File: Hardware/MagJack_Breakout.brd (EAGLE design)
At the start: 160 x 100 mm, 3 parts, among them J1 MAGJACK-NOLABELS

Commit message: Completed revised layout for prototypes
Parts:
- added FID1, FID2: FIDUCIAL1X2, SparkFun-Aesthetics:FIDUCIAL-1X2
- added LOGO1: OSHW-LOGOS, SparkFun-Aesthetics:OSHW-LOGO-S
- added LOGO2: SFE_LOGO_FLAME.1_INCH, SparkFun-Aesthetics:SFE_LOGO_FLAME_.1
- added LOGO3: SFE_LOGO_NAME_FLAME.1_INCH, SparkFun-Aesthetics:SFE_LOGO_NAME_FLAME_.1
- added STANDOFF3, STANDOFF5: STAND-OFF, SparkFun-Electromechanical:STAND-OFF
- moved J1 143.3 mm to (24.1, 25.4), turned to 180 degrees
- moved JP1 97.9 mm to (1.27, 1.27)
- moved FRAME1 80.1 mm to (-17.8, -10.2)
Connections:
- new net G+: J1.11, JP1.3
- new net G-: J1.12, JP1.2
- new net P1: J1.1, JP1.13
- new net P2: J1.2, JP1.12
- new net P3: J1.3, JP1.11
- new net P4: J1.4, JP1.10
- new net P5: J1.5, JP1.9
- new net P6: J1.6, JP1.8
- new net P7: J1.7, JP1.7
- new net P8: J1.8, JP1.6
- new net SH: J1.M1, J1.M2, JP1.1
- new net Y+: J1.9, JP1.5
- new net Y-: J1.10, JP1.4
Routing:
- net SH: track 0.00 -> 31.5 mm
- net Y+: track 0.00 -> 25.0 mm
- net Y-: track 0.00 -> 22.7 mm
- net G+: track 0.00 -> 20.4 mm
- net G-: track 0.00 -> 19.6 mm
- net P1: track 0.00 -> 13.6 mm
- net P3: track 0.00 -> 13.1 mm
- net P2: track 0.00 -> 11.2 mm
- net P5: track 0.00 -> 10.4 mm
- net P4: track 0.00 -> 9.42 mm
- net P7: track 0.00 -> 8.00 mm
- net P6: track 0.00 -> 6.28 mm
- net P8: track 0.00 -> 4.93 mm
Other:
- board size 160 x 100 mm -> 33 x 20.3 mm
- board text added: "G+"
- board text added: "G-"
- board text added: "P1"
- board text added: "P2\"
- board text added: "P3"
- board text added: "P4"
- board text added: "P5"
- board text added: "P6"
- board text added: "P7"
- board text added: "P8"
- board text added: "RJ45 MagJack Breakout"
- board text added: "Revised by Shawn Hymel"
- board text added: "SH"
- board text added: "Y+"
- board text added: "Y-"
- board text added: "v11"

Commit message: Added Nate as original designer
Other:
- board text added: "N. Seidle Revised by Shawn Hymel"
- board text removed: "Revised by Shawn Hymel"
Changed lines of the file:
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@@
 <text x="3.81" y="2.794" size="1.016" layer="21" font="vector" ratio="15" align="bottom-center">G-</text>
 <text x="1.27" y="2.794" size="1.016" layer="21" font="vector" ratio="15" align="bottom-center">SH</text>
-<text x="12.7" y="-10.3378" size="1.778" layer="51" font="vector">Revised by Shawn Hymel</text>
+<text x="12.7" y="-12.8778" size="1.778" layer="51" font="vector">N. Seidle
+Revised by Shawn Hymel</text>
 <text x="31.75" y="2.794" size="1.016" layer="22" font="vector" ratio="15" rot="MR0" align="bottom-center">P1</text>
 <text x="29.21" y="2.794" size="1.016" layer="22" font="vector" ratio="15" rot="MR0" align="bottom-center">P2\</text>

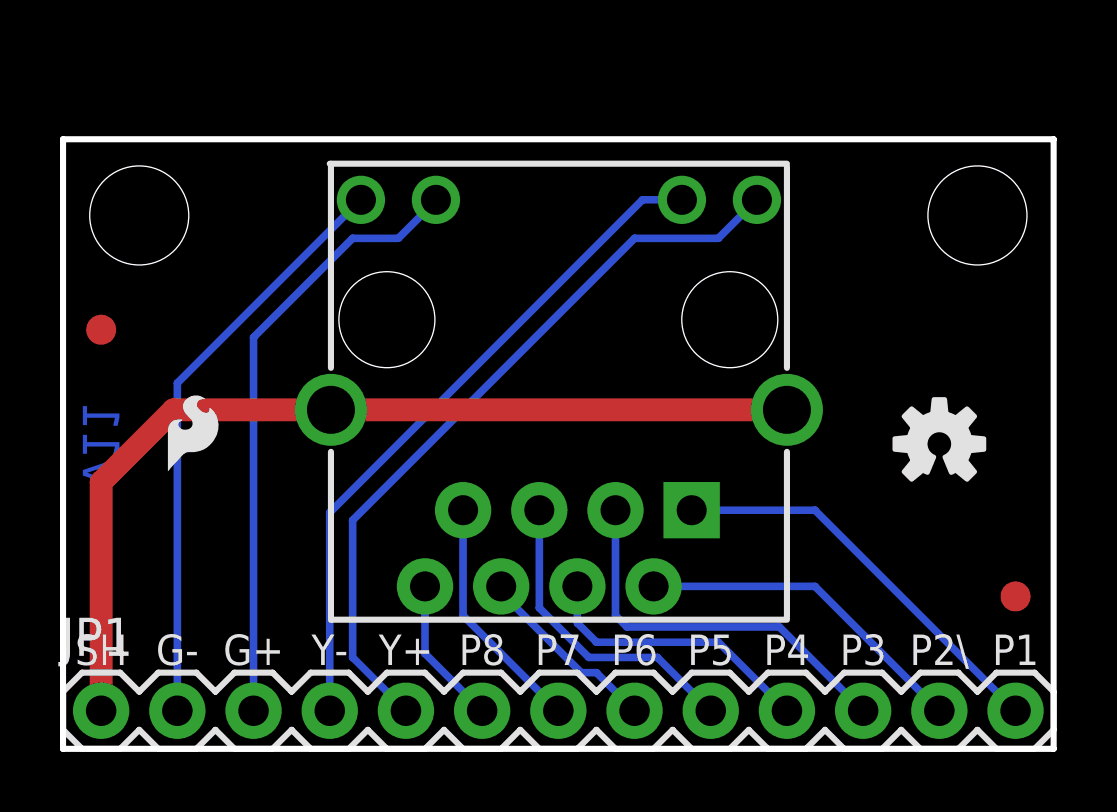
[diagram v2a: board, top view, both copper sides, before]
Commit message: Moved bottom/header section down by 0.1 in,
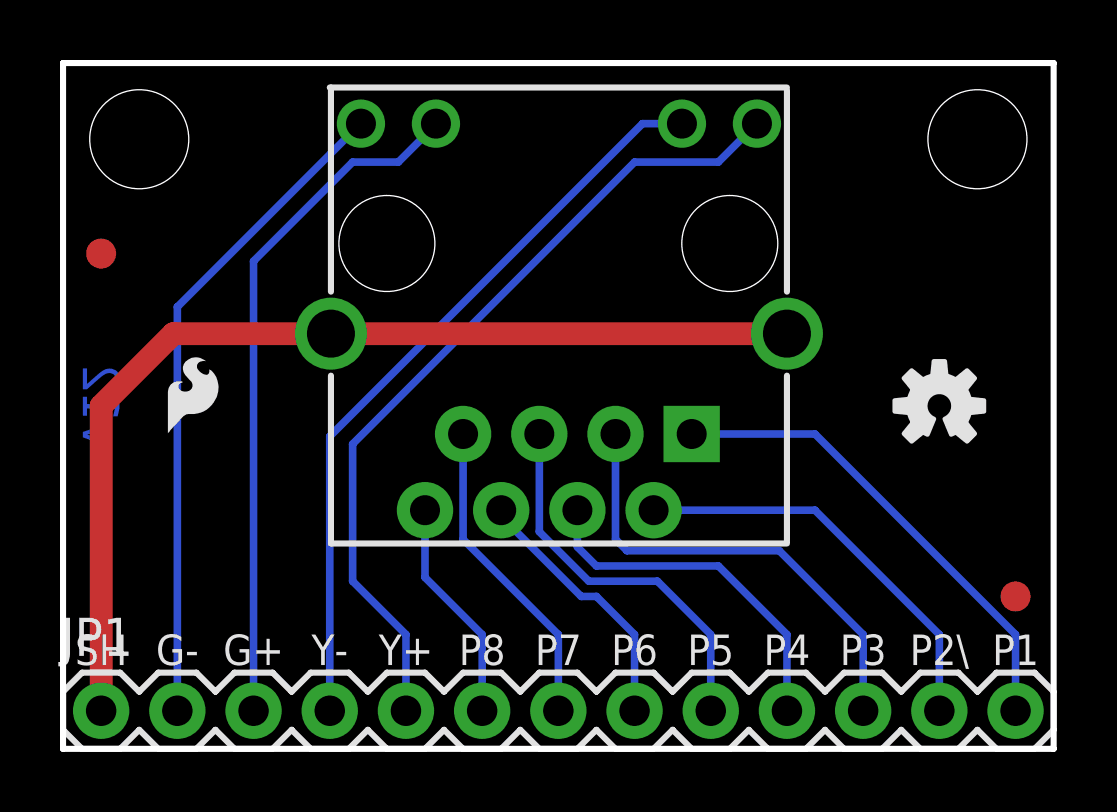
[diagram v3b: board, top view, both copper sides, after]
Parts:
- moved J1 2.54 mm to (24.1, 27.9)
- moved FID1 2.54 mm to (1.27, 16.5)
- moved LOGO3 2.54 mm to (22.5, 12.1)
- moved STANDOFF3 2.54 mm to (30.5, 20.3)
- moved STANDOFF5 2.54 mm to (2.54, 20.3)
- moved LOGO1 1.27 mm to (29.2, 11.4)
- moved LOGO2 1.27 mm to (3.17, 10.2)
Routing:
- net SH: track 31.5 -> 34.0 mm
- net P8: track 4.93 -> 7.47 mm
- net Y+: track 25.0 -> 27.5 mm
- net P7: track 8.00 -> 10.5 mm
- net P6: track 6.28 -> 8.82 mm
- net P5: track 10.4 -> 12.9 mm
- net P4: track 9.42 -> 12.0 mm
- net P2: track 11.2 -> 13.8 mm
- net G-: track 19.6 -> 22.1 mm
- net G+: track 20.4 -> 23.0 mm
- net P3: track 13.1 -> 15.6 mm
- net P1: track 13.6 -> 16.1 mm
- net Y-: track 22.7 -> 25.2 mm
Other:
- board size 33 x 20.3 mm -> 33 x 22.9 mm
- board text added: "v12"
- board text removed: "v11"

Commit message: Changed shield trace to top-side pour
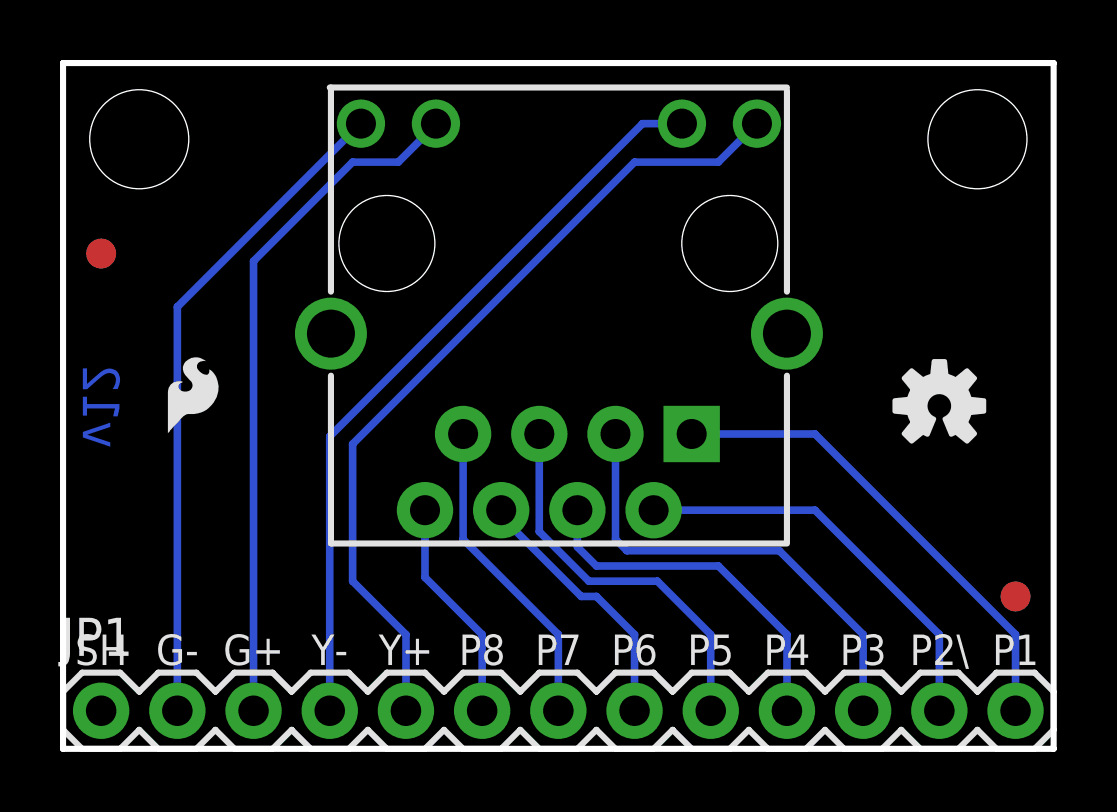
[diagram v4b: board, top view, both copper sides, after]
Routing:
- net SH: track 34.0 -> 0.00 mm
- added copper zone on layer 1, net SH
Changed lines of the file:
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@@
 <layer number="2" name="Route2" color="1" fill="3" visible="no" active="yes"/>
 <layer number="15" name="Route15" color="4" fill="6" visible="no" active="yes"/>
-<layer number="16" name="Bottom" color="1" fill="1" visible="yes" active="yes"/>
+<layer number="16" name="Bottom" color="1" fill="1" visible="no" active="yes"/>
 <layer number="17" name="Pads" color="2" fill="1" visible="yes" active="yes"/>
 <layer number="18" name="Vias" color="2" fill="1" visible="yes" active="yes"/>
@@
 <layer number="20" name="Dimension" color="15" fill="1" visible="yes" active="yes"/>
 <layer number="21" name="tPlace" color="16" fill="1" visible="yes" active="yes"/>
-<layer number="22" name="bPlace" color="14" fill="1" visible="yes" active="yes"/>
+<layer number="22" name="bPlace" color="14" fill="1" visible="no" active="yes"/>
 <layer number="23" name="tOrigins" color="15" fill="1" visible="yes" active="yes"/>
-<layer number="24" name="bOrigins" color="15" fill="1" visible="yes" active="yes"/>
+<layer number="24" name="bOrigins" color="15" fill="1" visible="no" active="yes"/>
 <layer number="25" name="tNames" color="7" fill="1" visible="no" active="yes"/>
 <layer number="26" name="bNames" color="7" fill="1" visible="no" active="yes"/>
@@
 <layer number="43" name="vRestrict" color="2" fill="10" visible="no" active="yes"/>
 <layer number="44" name="Drills" color="7" fill="1" visible="no" active="yes"/>
-<layer number="45" name="Holes" color="7" fill="1" visible="yes" active="yes"/>
+<layer number="45" name="Holes" color="7" fill="1" visible="no" active="yes"/>
 <layer number="46" name="Milling" color="3" fill="1" visible="no" active="yes"/>
-<layer number="51" name="tDocu" color="6" fill="1" visible="yes" active="yes"/>
+<layer number="51" name="tDocu" color="6" fill="1" visible="no" active="yes"/>
 <layer number="52" name="bDocu" color="7" fill="1" visible="no" active="yes"/>
 <layer number="3" name="Route3" color="4" fill="3" visible="no" active="no"/>
@@
 <contactref element="J1" pad="M2"/>
 <contactref element="JP1" pad="1"/>
-<wire x1="24.13" y1="13.84" x2="8.93" y2="13.84" width="0.762" layer="1"/>
-<wire x1="8.93" y1="13.84" x2="3.68" y2="13.84" width="0.762" layer="1"/>
-<wire x1="3.68" y1="13.84" x2="1.27" y2="11.43" width="0.762" layer="1"/>
-<wire x1="1.27" y1="11.43" x2="1.27" y2="1.27" width="0.762" layer="1"/>
+<polygon width="0.254" layer="1" isolate="0.3048">
+<vertex x="0" y="22.86"/>
+<vertex x="33.02" y="22.86"/>
+<vertex x="33.02" y="0"/>
+<vertex x="0" y="0"/>
+</polygon>
 </signal>
 <signal name="Y+">

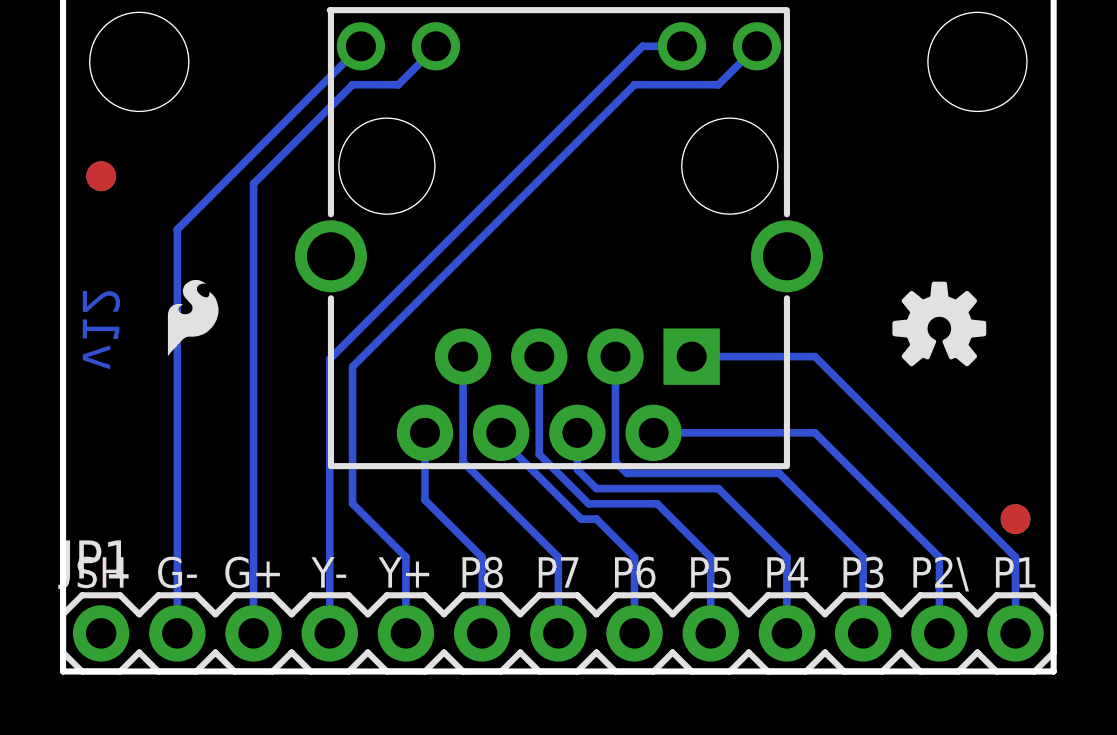
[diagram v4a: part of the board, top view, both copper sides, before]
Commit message: Added locking header
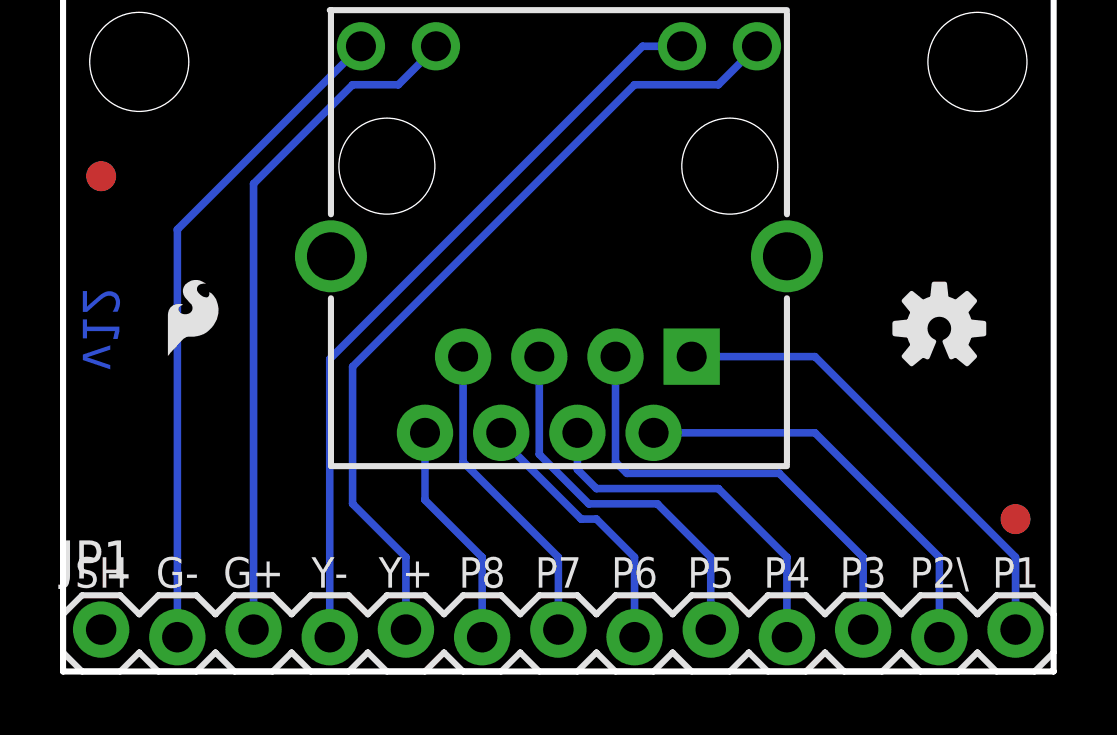
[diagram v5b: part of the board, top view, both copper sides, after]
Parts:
- JP1: value M13 -> M13LOCK; device SparkFun-Connectors:1X13 -> SparkFun-Connectors:1X13_LOCK
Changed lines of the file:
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@@
 <setting verticaltext="up"/>
 </settings>
-<grid distance="0.1" unitdist="inch" unit="inch" style="dots" multiple="1" display="yes" altdistance="0.05" altunitdist="inch" altunit="inch"/>
+<grid distance="0.05" unitdist="inch" unit="inch" style="dots" multiple="1" display="yes" altdistance="0.005" altunitdist="inch" altunit="inch"/>
 <layers>
 <layer number="1" name="Top" color="4" fill="1" visible="yes" active="yes"/>
 <layer number="2" name="Route2" color="1" fill="3" visible="no" active="yes"/>
 <layer number="15" name="Route15" color="4" fill="6" visible="no" active="yes"/>
-<layer number="16" name="Bottom" color="1" fill="1" visible="no" active="yes"/>
+<layer number="16" name="Bottom" color="1" fill="1" visible="yes" active="yes"/>
 <layer number="17" name="Pads" color="2" fill="1" visible="yes" active="yes"/>
 <layer number="18" name="Vias" color="2" fill="1" visible="yes" active="yes"/>
@@
 <layer number="20" name="Dimension" color="15" fill="1" visible="yes" active="yes"/>
 <layer number="21" name="tPlace" color="16" fill="1" visible="yes" active="yes"/>
-<layer number="22" name="bPlace" color="14" fill="1" visible="no" active="yes"/>
+<layer number="22" name="bPlace" color="14" fill="1" visible="yes" active="yes"/>
 <layer number="23" name="tOrigins" color="15" fill="1" visible="yes" active="yes"/>
-<layer number="24" name="bOrigins" color="15" fill="1" visible="no" active="yes"/>
+<layer number="24" name="bOrigins" color="15" fill="1" visible="yes" active="yes"/>
 <layer number="25" name="tNames" color="7" fill="1" visible="no" active="yes"/>
 <layer number="26" name="bNames" color="7" fill="1" visible="no" active="yes"/>
@@
 <layer number="43" name="vRestrict" color="2" fill="10" visible="no" active="yes"/>
 <layer number="44" name="Drills" color="7" fill="1" visible="no" active="yes"/>
-<layer number="45" name="Holes" color="7" fill="1" visible="no" active="yes"/>
+<layer number="45" name="Holes" color="7" fill="1" visible="yes" active="yes"/>
 <layer number="46" name="Milling" color="3" fill="1" visible="no" active="yes"/>
-<layer number="51" name="tDocu" color="6" fill="1" visible="no" active="yes"/>
+<layer number="51" name="tDocu" color="6" fill="1" visible="yes" active="yes"/>
 <layer number="52" name="bDocu" color="7" fill="1" visible="no" active="yes"/>
 <layer number="3" name="Route3" color="4" fill="3" visible="no" active="no"/>
@@
 <param name="dpGapFactor" value="2.5"/>
 <param name="checkGrid" value="0"/>
-<param name="checkAngle" value="1"/>
+<param name="checkAngle" value="0"/>
 <param name="checkFont" value="1"/>
 <param name="checkRestrict" value="1"/>
@@
 <elements>
 <element name="FRAME1" library="SparkFun-Aesthetics" package="CREATIVE_COMMONS" value="FRAME-LETTER" x="-17.78" y="-10.16"/>
-<element name="JP1" library="SparkFun-Connectors" package="1X13" value="M13" x="1.27" y="1.27"/>
+<element name="JP1" library="SparkFun-Connectors" package="1X13_LOCK" value="M13LOCK" x="1.27" y="1.27"/>
 <element name="J1" library="SparkFun-Connectors" package="MAGJACK" value="MAGJACK-NOLABELS" x="24.13" y="27.94" rot="R180">
 <attribute name="PROD_ID" value="CONN-09556" x="24.13" y="27.94" size="1.778" layer="27" font="vector" ratio="15" rot="R180" display="off"/>
@@
 <contactref element="JP1" pad="13"/>
 <wire x1="20.955" y1="10.495" x2="25.065" y2="10.495" width="0.254" layer="16"/>
-<wire x1="31.75" y1="1.27" x2="31.75" y2="3.81" width="0.254" layer="16"/>
+<wire x1="31.75" y1="1.397" x2="31.75" y2="3.81" width="0.254" layer="16"/>
 <wire x1="31.75" y1="3.81" x2="25.065" y2="10.495" width="0.254" layer="16"/>
 </signal>
@@
 <contactref element="JP1" pad="12"/>
 <wire x1="19.685" y1="7.955" x2="25.065" y2="7.955" width="0.254" layer="16"/>
-<wire x1="29.21" y1="1.27" x2="29.21" y2="3.81" width="0.254" layer="16"/>
+<wire x1="29.21" y1="1.143" x2="29.21" y2="3.81" width="0.254" layer="16"/>
 <wire x1="29.21" y1="3.81" x2="25.065" y2="7.955" width="0.254" layer="16"/>
 </signal>
@@
 <wire x1="18.415" y1="6.985" x2="18.796" y2="6.604" width="0.254" layer="16"/>
 <wire x1="18.796" y1="6.604" x2="23.876" y2="6.604" width="0.254" layer="16"/>
-<wire x1="26.67" y1="1.27" x2="26.67" y2="3.81" width="0.254" layer="16"/>
+<wire x1="26.67" y1="1.397" x2="26.67" y2="3.81" width="0.254" layer="16"/>
 <wire x1="26.67" y1="3.81" x2="23.876" y2="6.604" width="0.254" layer="16"/>
 </signal>
@@
 <wire x1="17.145" y1="6.731" x2="17.78" y2="6.096" width="0.254" layer="16"/>
 <wire x1="17.78" y1="6.096" x2="21.844" y2="6.096" width="0.254" layer="16"/>
-<wire x1="24.13" y1="1.27" x2="24.13" y2="3.81" width="0.254" layer="16"/>
+<wire x1="24.13" y1="1.143" x2="24.13" y2="3.81" width="0.254" layer="16"/>
 <wire x1="24.13" y1="3.81" x2="21.844" y2="6.096" width="0.254" layer="16"/>
 </signal>
@@
 <wire x1="15.875" y1="7.239" x2="17.526" y2="5.588" width="0.254" layer="16"/>
 <wire x1="17.526" y1="5.588" x2="19.812" y2="5.588" width="0.254" layer="16"/>
-<wire x1="21.59" y1="1.27" x2="21.59" y2="3.81" width="0.254" layer="16"/>
+<wire x1="21.59" y1="1.397" x2="21.59" y2="3.81" width="0.254" layer="16"/>
 <wire x1="21.59" y1="3.81" x2="19.812" y2="5.588" width="0.254" layer="16"/>
 </signal>
@@
 <wire x1="14.605" y1="7.747" x2="17.272" y2="5.08" width="0.254" layer="16"/>
 <wire x1="17.272" y1="5.08" x2="17.78" y2="5.08" width="0.254" layer="16"/>
-<wire x1="19.05" y1="1.27" x2="19.05" y2="3.81" width="0.254" layer="16"/>
+<wire x1="19.05" y1="1.143" x2="19.05" y2="3.81" width="0.254" layer="16"/>
 <wire x1="19.05" y1="3.81" x2="17.78" y2="5.08" width="0.254" layer="16"/>
 </signal>
@@
 <contactref element="JP1" pad="7"/>
 <wire x1="13.335" y1="10.495" x2="13.335" y2="6.985" width="0.254" layer="16"/>
-<wire x1="16.51" y1="1.27" x2="16.51" y2="3.81" width="0.254" layer="16"/>
+<wire x1="16.51" y1="1.397" x2="16.51" y2="3.81" width="0.254" layer="16"/>
 <wire x1="16.51" y1="3.81" x2="13.335" y2="6.985" width="0.254" layer="16"/>
 </signal>
@@
 <contactref element="JP1" pad="6"/>
 <wire x1="12.065" y1="7.955" x2="12.065" y2="5.715" width="0.254" layer="16"/>
-<wire x1="13.97" y1="1.27" x2="13.97" y2="3.81" width="0.254" layer="16"/>
+<wire x1="13.97" y1="1.143" x2="13.97" y2="3.81" width="0.254" layer="16"/>
 <wire x1="13.97" y1="3.81" x2="12.065" y2="5.715" width="0.254" layer="16"/>
 </signal>
@@
 <wire x1="19.05" y1="19.558" x2="9.652" y2="10.16" width="0.254" layer="16"/>
 <wire x1="9.652" y1="10.16" x2="9.652" y2="5.588" width="0.254" layer="16"/>
-<wire x1="11.43" y1="1.27" x2="11.43" y2="3.81" width="0.254" layer="16"/>
+<wire x1="11.43" y1="1.397" x2="11.43" y2="3.81" width="0.254" layer="16"/>
 <wire x1="11.43" y1="3.81" x2="9.652" y2="5.588" width="0.254" layer="16"/>
 </signal>
@@
 <wire x1="20.63" y1="20.84" x2="19.316" y2="20.84" width="0.254" layer="16"/>
 <wire x1="19.316" y1="20.84" x2="8.89" y2="10.414" width="0.254" layer="16"/>
-<wire x1="8.89" y1="10.414" x2="8.89" y2="1.27" width="0.254" layer="16"/>
+<wire x1="8.89" y1="10.414" x2="8.89" y2="1.143" width="0.254" layer="16"/>
 </signal>
 <signal name="G+">
@@
 <wire x1="11.176" y1="19.558" x2="9.652" y2="19.558" width="0.254" layer="16"/>
 <wire x1="9.652" y1="19.558" x2="6.35" y2="16.256" width="0.254" layer="16"/>
-<wire x1="6.35" y1="16.256" x2="6.35" y2="1.27" width="0.254" layer="16"/>
+<wire x1="6.35" y1="16.256" x2="6.35" y2="1.397" width="0.254" layer="16"/>
 </signal>
 <signal name="G-">
@@
 <wire x1="9.93" y1="20.84" x2="9.918" y2="20.84" width="0.254" layer="16"/>
 <wire x1="9.918" y1="20.84" x2="3.81" y2="14.732" width="0.254" layer="16"/>
-<wire x1="3.81" y1="14.732" x2="3.81" y2="1.27" width="0.254" layer="16"/>
+<wire x1="3.81" y1="14.732" x2="3.81" y2="1.143" width="0.254" layer="16"/>
 </signal>
 </signals>
